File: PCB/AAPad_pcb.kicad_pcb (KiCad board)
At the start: 2 copper layers, 85.7 x 81 mm, 31 parts, among them J1 OLED_DISPLAY, SW1 SW_Push_45deg, SW11 RotaryEncoder_Switch, SW2 SW_Push_45deg, SW3 SW_Push_45deg, SW4 SW_Push_45deg, SW5 SW_Push_45deg, SW6 SW_Push_45deg, SW7 SW_Push_45deg, SW8 SW_Push_45deg, U1 XIAO-RP2040-DIP

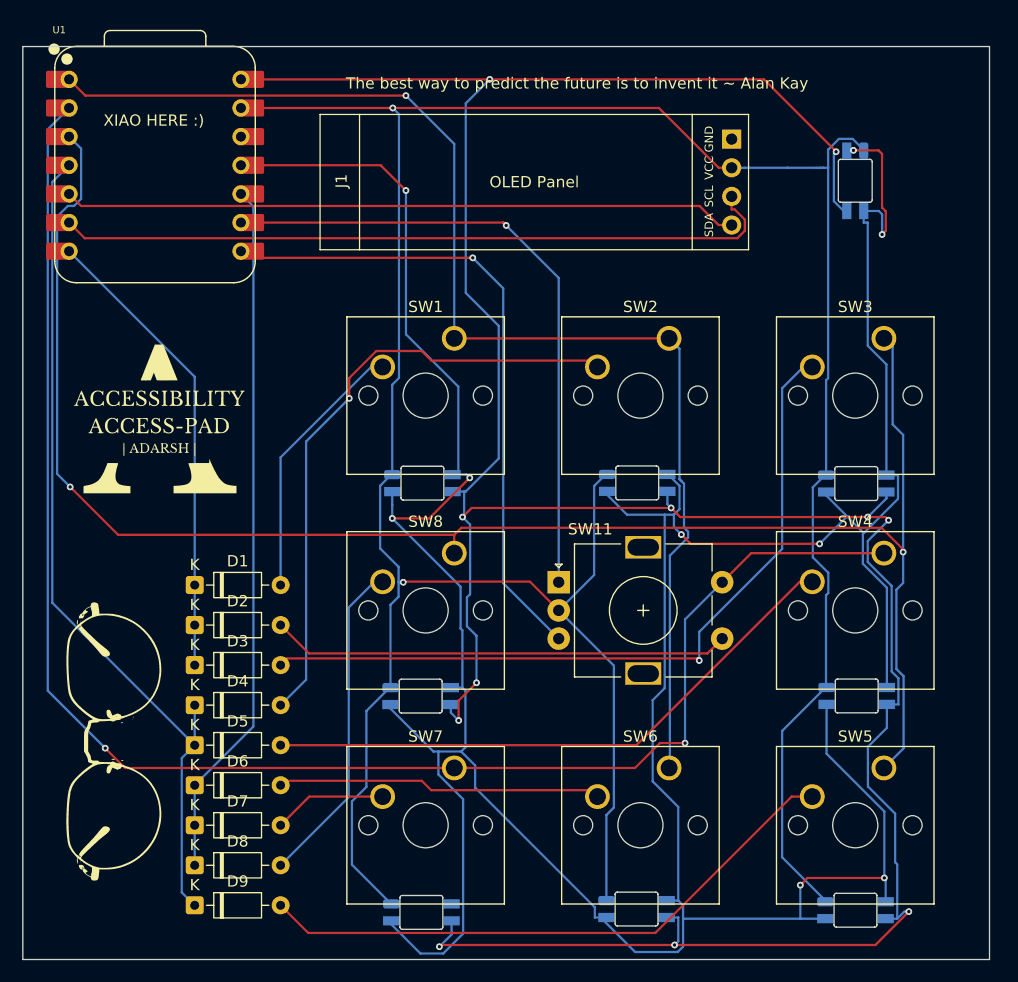
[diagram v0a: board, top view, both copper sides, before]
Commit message: Added Gerber Files for Production, ReadMe complete
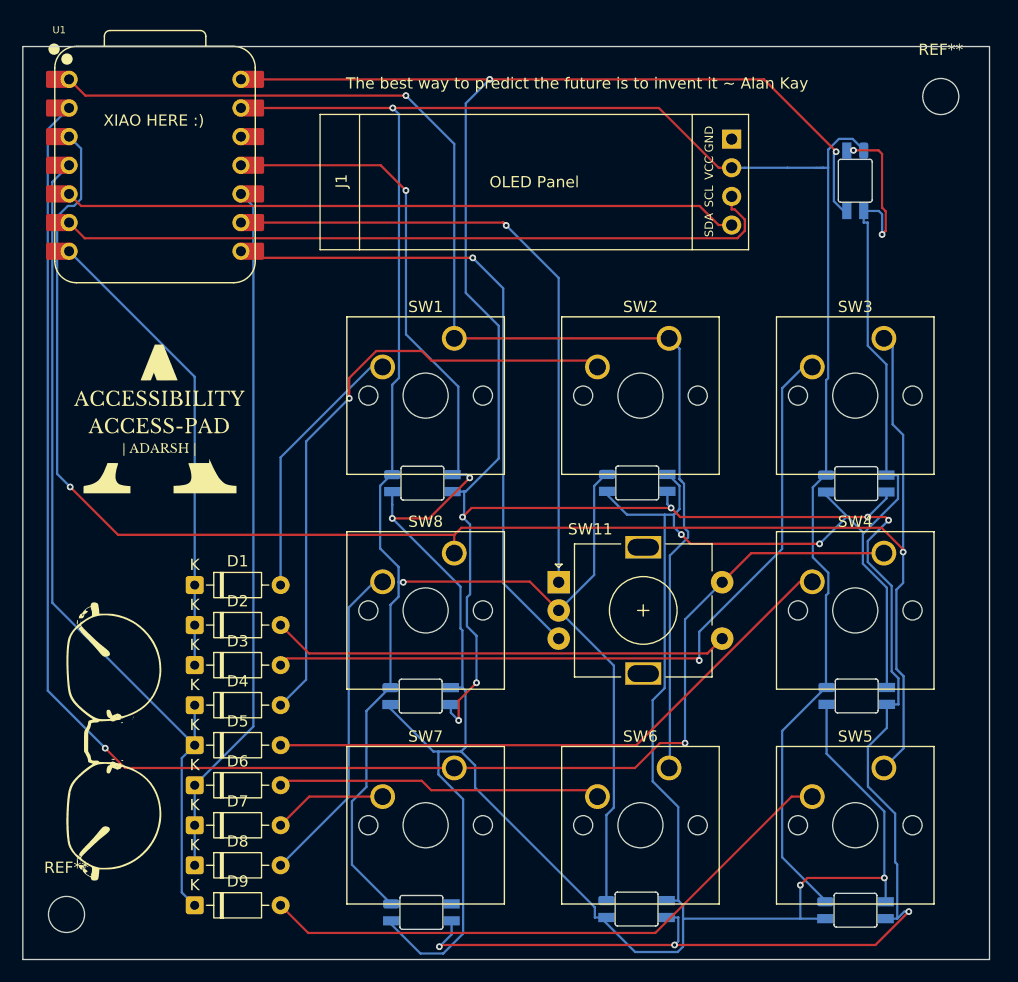
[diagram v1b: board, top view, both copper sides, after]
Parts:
- added REF**: MountingHole_3.2mm_M3, MountingHole:MountingHole_3.2mm_M3, F.Cu at (61.0, 112.7)
- added REF**: MountingHole_3.2mm_M3, MountingHole:MountingHole_3.2mm_M3, F.Cu at (138.6, 40.2)
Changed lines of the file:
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@@
 			(outputformat 1)
 			(mirror no)
-			(drillshape 1)
+			(drillshape 0)
 			(scaleselection 1)
-			(outputdirectory "")
+			(outputdirectory "../Production/Gerber Files/")
 		)
 	)
@@
 		)
 	)
+	(footprint "MountingHole:MountingHole_3.2mm_M3"
+		(layer "F.Cu")
+		(at 61.022763 112.685612)
+		(descr "Mounting Hole 3.2mm, M3, no annular, generated by kicad-footprint-generator mountinghole.py")
+		(tags "mountinghole M3")
+		(property "Reference" "REF**"
+			(at 0 -4.15 0)
+			(layer "F.SilkS")
+			(effects
+				(font
+					(size 1 1)
+					(thickness 0.15)
+				)
+			)
+		)
+		(property "Value" "MountingHole_3.2mm_M3"
+			(at 0 4.15 0)
+			(layer "F.Fab")
+			(effects
+				(font
+					(size 1 1)
+					(thickness 0.15)
+				)
+			)
+		)
+		(property "Datasheet" ""
+			(at 0 0 0)
+			(layer "F.Fab")
+			(hide yes)
+			(effects
+				(font
+					(size 1.27 1.27)
+					(thickness 0.15)
+				)
+			)
+		)
+		(property "Description" ""
+			(at 0 0 0)
+			(layer "F.Fab")
+			(hide yes)
+			(effects
+				(font
+					(size 1.27 1.27)
+					(thickness 0.15)
+				)
+			)
+		)
+		(attr exclude_from_pos_files exclude_from_bom)
+		(fp_circle
+			(center 0 0)
+			(end 3.2 0)
+			(stroke
+				(width 0.15)
+				(type solid)
+			)
+			(fill no)
+			(layer "Cmts.User")
+		)
+		(fp_circle
+			(center 0 0)
+			(end 3.45 0)
+			(stroke
+				(width 0.05)
+				(type solid)
+			)
+			(fill no)
+			(layer "F.CrtYd")
+		)
+		(fp_text user "${REFERENCE}"
+			(at 0 0 0)
+			(layer "F.Fab")
+			(effects
+				(font
+					(size 1 1)
+					(thickness 0.15)
+				)
+			)
+		)
+		(pad "" np_thru_hole circle
+			(at 0 0)
+			(size 3.2 3.2)
+			(drill 3.2)
+			(layers "*.Cu" "*.Mask")
+		)
+		(embedded_fonts no)
+	)
 	(footprint "Diode_THT:D_DO-35_SOD27_P7.62mm_Horizontal"
 		(layer "F.Cu")
@@
 		)
 	)
+	(footprint "MountingHole:MountingHole_3.2mm_M3"
+		(layer "F.Cu")
+		(at 138.552836 40.150997)
+		(descr "Mounting Hole 3.2mm, M3, no annular, generated by kicad-footprint-generator mountinghole.py")
+		(tags "mountinghole M3")
+		(property "Reference" "REF**"
+			(at 0 -4.15 0)
+			(layer "F.SilkS")
+			(effects
+				(font
+					(size 1 1)
+					(thickness 0.15)
+				)
+			)
+		)
+		(property "Value" "MountingHole_3.2mm_M3"
+			(at 0 4.15 0)
+			(layer "F.Fab")
+			(effects
+				(font
+					(size 1 1)
+					(thickness 0.15)
+				)
+			)
+		)
+		(property "Datasheet" ""
+			(at 0 0 0)
+			(layer "F.Fab")
+			(hide yes)
+			(effects
+				(font
+					(size 1.27 1.27)
+					(thickness 0.15)
+				)
+			)
+		)
+		(property "Description" ""
+			(at 0 0 0)
+			(layer "F.Fab")
+			(hide yes)
+			(effects
+				(font
+					(size 1.27 1.27)
+					(thickness 0.15)
+				)
+			)
+		)
+		(attr exclude_from_pos_files exclude_from_bom)
+		(fp_circle
+			(center 0 0)
+			(end 3.2 0)
+			(stroke
+				(width 0.15)
+				(type solid)
+			)
+			(fill no)
+			(layer "Cmts.User")
+		)
+		(fp_circle
+			(center 0 0)
+			(end 3.45 0)
+			(stroke
+				(width 0.05)
+				(type solid)
+			)
+			(fill no)
+			(layer "F.CrtYd")
+		)
+		(fp_text user "${REFERENCE}"
+			(at 0 0 0)
+			(layer "F.Fab")
+			(effects
+				(font
+					(size 1 1)
+					(thickness 0.15)
+				)
+			)
+		)
+		(pad "" np_thru_hole circle
+			(at 0 0)
+			(size 3.2 3.2)
+			(drill 3.2)
+			(layers "*.Cu" "*.Mask")
+		)
+		(embedded_fonts no)
+	)
 	(footprint "Button_Switch_Keyboard:SW_Cherry_MX_1.00u_PCB"
